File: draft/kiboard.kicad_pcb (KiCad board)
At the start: 2 copper layers, 125 x 100.7 mm, 35 parts

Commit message: Routing and edge cuts
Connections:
- net P1 renamed Switch01
- net P10 renamed Switch17
- net P19 renamed Switch08
- net P8 renamed Switch15
- net P9 renamed Switch16
- MCU1 pad 10: P14 -> Switch14
- MCU1 pad 15: P7 -> Switch13
- MCU1 pad 16: P6 -> Switch11
- MCU1 pad 17: P5 -> Switch09
- MCU1 pad 18: P4 -> Switch07
- MCU1 pad 19: P3 -> Switch05
- MCU1 pad 20: P2 -> Switch03
- MCU1 pad 23: P0 -> Switch02
- MCU1 pad 5: P21 -> Switch04
- MCU1 pad 6: P20 -> Switch06
- MCU1 pad 8: P18 -> Switch10
- MCU1 pad 9: P15 -> Switch12
- S1 pad 1: P2 -> Switch11
- S10 pad 1: P3 -> Switch07
- S11 pad 1: P21 -> Switch02
- S12 pad 1: P21 -> Switch02
- S13 pad 1: P5 -> Switch13
- S14 pad 1: P5 -> Switch13
- S17 pad 1: P4 -> Switch03
- S18 pad 1: P4 -> Switch03
- S19 pad 1: P15 -> Switch14
- S2 pad 1: P2 -> Switch11
- S20 pad 1: P15 -> Switch14
- S21 pad 1: P6 -> Switch09
- S22 pad 1: P6 -> Switch09
- S23 pad 1: P18 -> Switch04
- S24 pad 1: P18 -> Switch04
- S27 pad 1: P14 -> Switch10
- S28 pad 1: P14 -> Switch10
- S29 pad 1: P7 -> Switch05
- S3 pad 1: P0 -> Switch06
- S30 pad 1: P7 -> Switch05
- S4 pad 1: P0 -> Switch06
- S7 pad 1: P20 -> Switch12
- S8 pad 1: P20 -> Switch12
- S9 pad 1: P3 -> Switch07
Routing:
- net GND: track 0.00 -> 816.0 mm
- net Switch05: track 0.00 -> 156.4 mm
- net Switch10: track 0.00 -> 139.0 mm
- net Switch15: track 0.00 -> 136.3 mm
- net Switch09: track 0.00 -> 122.9 mm
- net Switch04: track 0.00 -> 119.4 mm
- net Switch14: track 0.00 -> 113.5 mm
- net Switch03: track 0.00 -> 105.4 mm
- net Switch08: track 0.00 -> 99.0 mm
- net Switch13: track 0.00 -> 97.8 mm
- net Switch02: track 0.00 -> 73.9 mm
- net Switch07: track 0.00 -> 72.8 mm
- net Switch12: track 0.00 -> 72.6 mm
- net Switch17: track 0.00 -> 55.3 mm
- net Switch01: track 0.00 -> 53.4 mm
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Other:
- board size 125 x 100.7 mm -> 127.3 x 101 mm

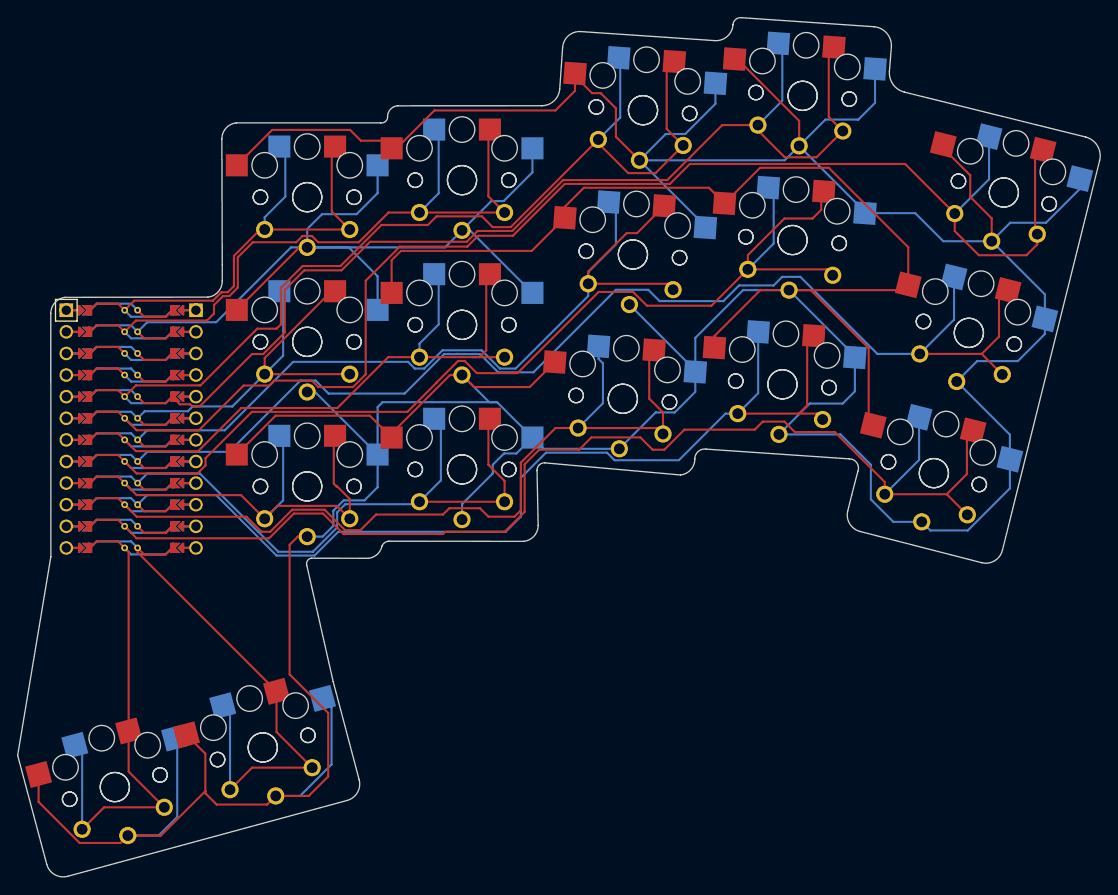
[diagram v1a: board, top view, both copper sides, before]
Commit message: Added footprints from Ben Vallack's designs and modified routing a bit
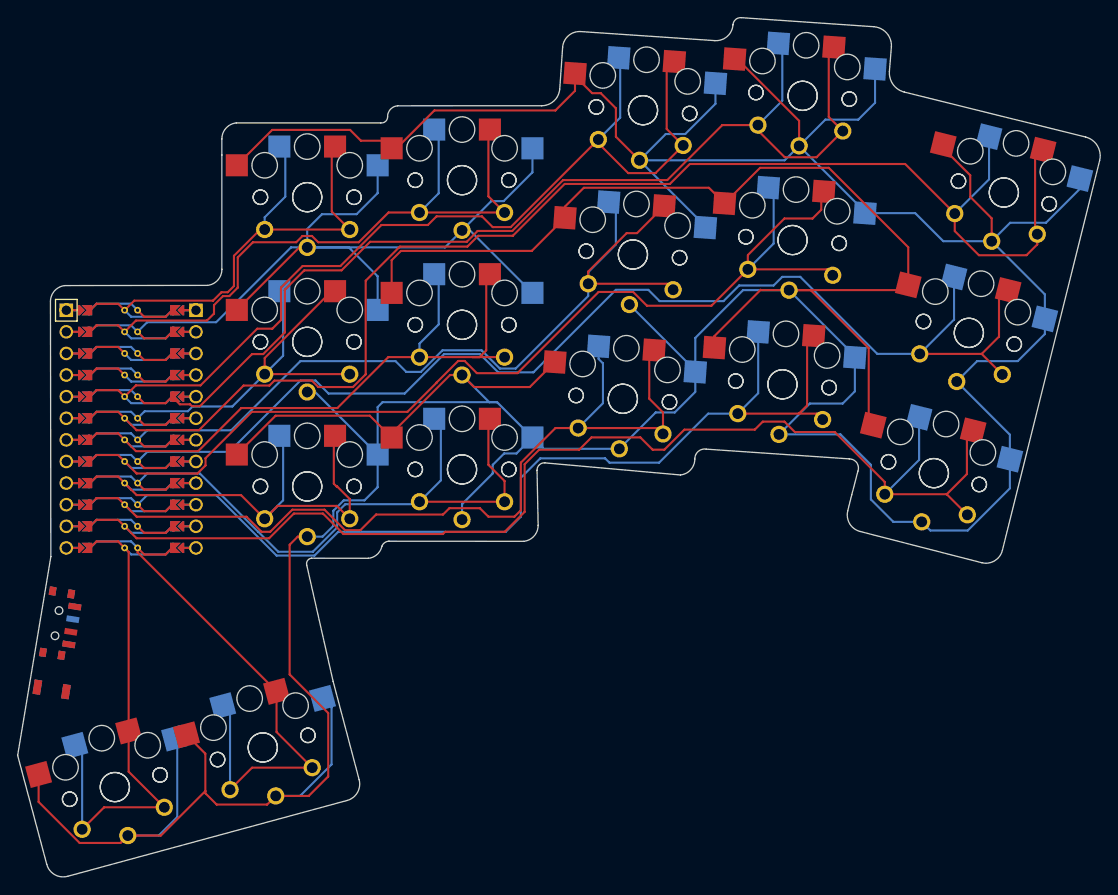
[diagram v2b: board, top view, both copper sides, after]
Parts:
- added ?: , SW_SPST_B3U-1000P-Ben-Vallack, F.Cu at (-13.2, 23.9)
- added ?: , SW_SPDT_PCM12-Ben-Vallack, F.Cu at (-12.3, 16.1)
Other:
- outline, holes or cut-outs redrawn

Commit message: Finished routing
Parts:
- added ?: , lib:bat, F.Cu at (-4.12, 12.7)
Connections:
- ? pad 1: (no net) -> pos
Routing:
- net RST: track 0.00 -> 69.2 mm, vias 0 -> 5
- net RAW: track 0.00 -> 58.2 mm, vias 0 -> 1
- net GND: track 816.0 -> 864.0 mm
- net pos: track 0.00 -> 22.4 mm
- net Switch16: track 53.4 -> 61.1 mm
- net Switch11: track 50.9 -> 53.4 mm
- net Switch10: track 139.0 -> 140.5 mm
- net Switch09: track 122.9 -> 124.2 mm
- net Switch04: track 119.4 -> 120.7 mm
- net Switch13: track 97.8 -> 98.4 mm

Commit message: Added more products to README and finished up the first draft
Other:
- board text added: "KIBOARD 001-DRAFT"
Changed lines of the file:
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@@
   (gr_arc (start 43.815 -1.905) (mid 44.083856 -2.536244) (end 44.728806 -2.770146) (layer "Edge.Cuts") (width 0.15))
   (gr_arc (start 26.249999 -43.459349) (mid 26.585537 -44.334121) (end 27.433904 -44.740295) (layer "Edge.Cuts") (width 0.15))
+  (gr_text "KIBOARD 001-DRAFT" (at 3.048 22.86 14) (layer "B.SilkS")
+    (effects (font (size 1.5 1.5) (thickness 0.15)) (justify mirror))
+  )
+  (gr_text "KIBOARD 001-DRAFT" (at 3.048 22.86 14) (layer "F.SilkS")
+    (effects (font (size 1.5 1.5) (thickness 0.15)))
+  )
   (segment (start 11.8 3.8) (end 13.314 2.286) (width 0.25) (layer "F.Cu") (net 1))
   (segment (start 20.246697 0) (end 19.924999 -0.321698) (width 0.25) (layer "F.Cu") (net 1))
